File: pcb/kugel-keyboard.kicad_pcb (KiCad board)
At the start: 2 copper layers, 120.5 x 85.5 mm, 34 parts, among them SW1 MX_SW_HS, SW10 MX_SW_HS, SW11 MX_SW_HS, SW12 MX_SW_HS, SW13 MX_SW_HS, SW14 MX_SW_HS, SW15 MX_SW_HS, SW16 MX_SW_HS, SW17 MX_SW_HS, SW2 MX_SW_HS, SW3 MX_SW_HS, SW4 MX_SW_HS, SW5 MX_SW_HS, SW6 MX_SW_HS, SW7 MX_SW_HS, SW8 MX_SW_HS, SW9 MX_SW_HS

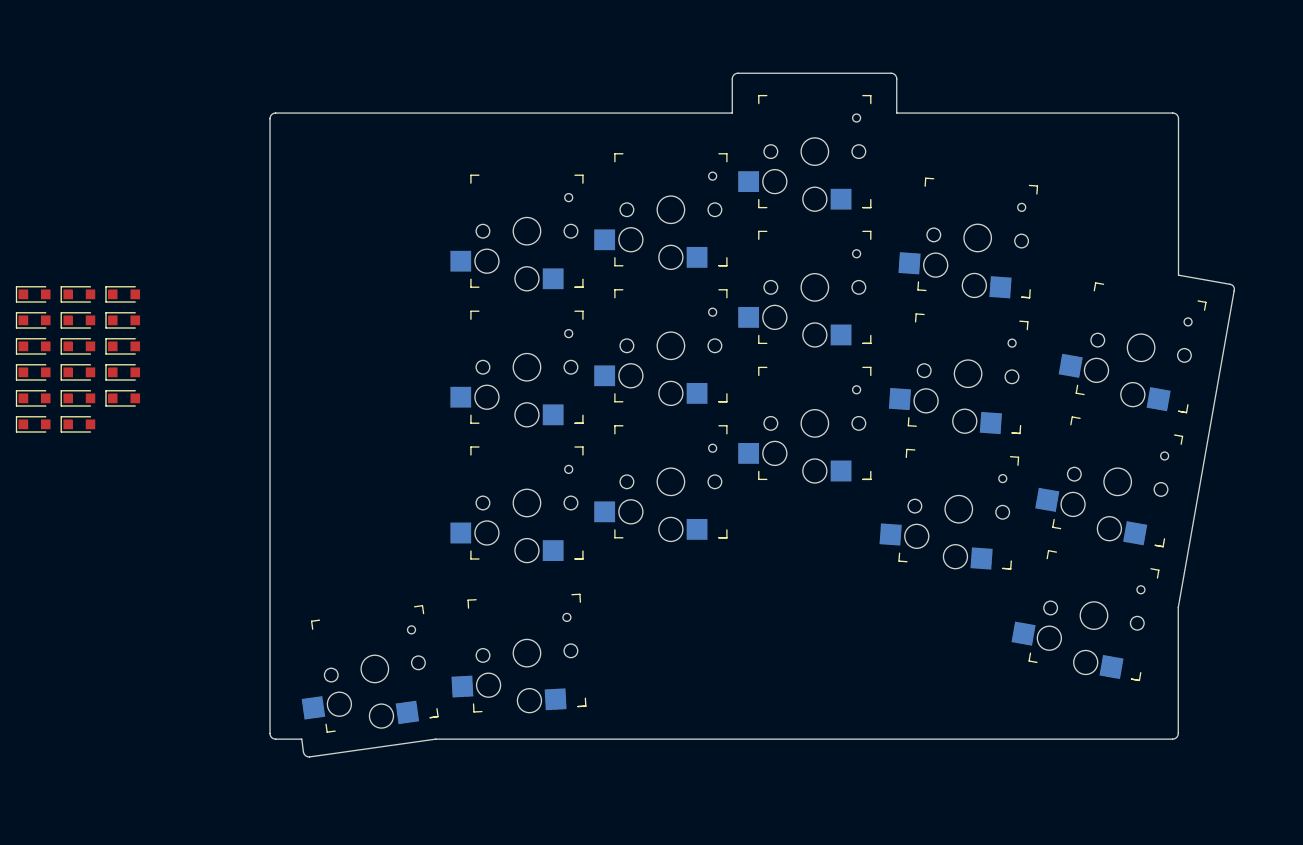
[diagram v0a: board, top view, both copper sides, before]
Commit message: added right side PCB and GPIO breakout PCB
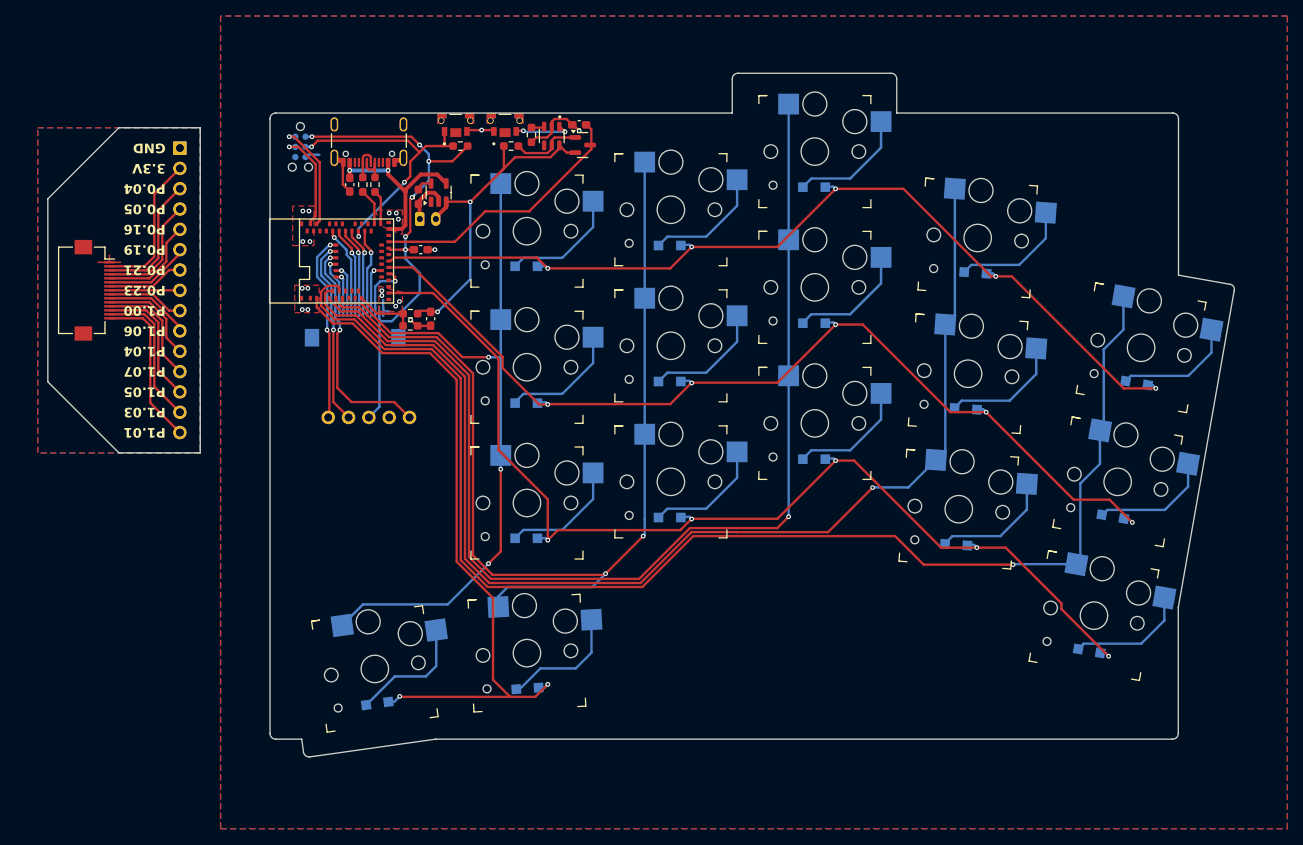
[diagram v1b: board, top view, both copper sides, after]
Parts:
- added C1: 10u, Capacitor_SMD:C_0603_1608Metric_Pad1.08x0.95mm_HandSolder, F.Cu at (117.8, 65.5)
- added C2: 10u, Capacitor_SMD:C_0603_1608Metric_Pad1.08x0.95mm_HandSolder, F.Cu at (127.9, 82.3)
- added C3: 10u, Capacitor_SMD:C_0603_1608Metric_Pad1.08x0.95mm_HandSolder, F.Cu at (126.6, 73.7)
- added C4: 10u, Capacitor_SMD:C_0603_1608Metric_Pad1.08x0.95mm_HandSolder, F.Cu at (146.4, 58.1)
- added J1: Conn_01x15_Pin, Connector_FFC-FPC:Hirose_FH12-15S-0.5SH_1x15-1MP_P0.50mm_Horizontal, F.Cu at (85.9, 78.7)
- added J2: USB_C_Receptacle_USB2.0_16P, Connector_USB:USB_C_Receptacle_GCT_USB4105-xx-A_16P_TopMnt_Horizontal, F.Cu at (120.1, 59.1)
- added J3: Conn_01x02_Socket, custom-libary:Battery_solder_pads, F.Cu at (126.5, 69.8)
- added J4: Conn_01x15_Pin, Connector_PinHeader_2.54mm:PinHeader_1x15_P2.54mm_Vertical, B.Cu at (96.5, 61.0)
- added J5: Conn_ARM_SWD_TagConnect_TC2030-NL, Connector:Tag-Connect_TC2030-IDC-NL_2x03_P1.27mm_Vertical, B.Cu at (111.6, 60.8)
- added J6: Conn_01x15_Pin, Connector_FFC-FPC:Hirose_FH12-15S-0.5SH_1x15-1MP_P0.50mm_Horizontal, B.Cu at (118.4, 83.3)
- added Q1: IRLML6402, Package_TO_SOT_SMD:SOT-23, F.Cu at (146.9, 60.6)
- added R1: 2k, Resistor_SMD:R_0603_1608Metric_Pad0.98x0.95mm_HandSolder, F.Cu at (126.3, 67.1)
- added R2: R, Resistor_SMD:R_0603_1608Metric_Pad0.98x0.95mm_HandSolder, F.Cu at (125.3, 81.7)
- added R3: R, Resistor_SMD:R_0603_1608Metric_Pad0.98x0.95mm_HandSolder, F.Cu at (125.3, 83.2)
- added R4: 27, Resistor_SMD:R_0603_1608Metric_Pad0.98x0.95mm_HandSolder, F.Cu at (120.9, 65.5)
- added R5: 27, Resistor_SMD:R_0603_1608Metric_Pad0.98x0.95mm_HandSolder, F.Cu at (119.4, 65.5)
- added R6: 100k, Resistor_SMD:R_0603_1608Metric_Pad0.98x0.95mm_HandSolder, F.Cu at (131.6, 60.7)
- added R7: 100k, Resistor_SMD:R_0603_1608Metric_Pad0.98x0.95mm_HandSolder, F.Cu at (140.5, 59.3)
- added R8: 100k, Resistor_SMD:R_0603_1608Metric_Pad0.98x0.95mm_HandSolder, F.Cu at (137.9, 60.7)
- added SW18: SW_Push, custom-libary:SW_TL6340AF160Q, F.Cu at (131.0, 57.5)
- added SW20: SW_Push, custom-libary:SW_TL6340AF160Q, F.Cu at (137.2, 57.5)
- added U1: MDBT50Q, custom-libary:MDBT50Q-1MV2, F.Cu at (123.2, 80.3)
- added U2: LTC4054ES5-4.2, Package_TO_SOT_SMD:TSOT-23-5, F.Cu at (128.9, 66.5)
- added U3: ~, custom-libary:nice!view, F.Cu at (115.1, 94.6)
- added U4: MAX16054AZT_T, custom-libary:SOT95P275X110-6N, F.Cu at (143.0, 59.5)
- D1, D10, D11, D12, D13, D14, D15, D16, D17, D2, D3, D4, D5, D6, D7, D8, D9: moved to B.Cu
- moved D15 126.7 mm to (216.1, 90.3), turned to 170 degrees
- moved D16 124.9 mm to (213.1, 107.0), turned to 170 degrees
- moved D17 124.7 mm to (210.2, 123.8), turned to 170 degrees
- moved D12 113.6 mm to (195.9, 76.6), turned to 176 degrees
- moved D14 107.7 mm to (193.6, 110.5), turned to 176 degrees
- moved D13 106.2 mm to (194.7, 93.6), turned to 176 degrees
- moved D9 94.0 mm to (175.8, 65.8), turned to 180 degrees
- moved D11 92.2 mm to (175.8, 99.8), turned to 180 degrees
- moved D10 92.1 mm to (175.8, 82.8), turned to 180 degrees
- moved D5 81.7 mm to (157.7, 73.1), turned to 180 degrees
- moved D6 79.6 mm to (157.7, 90.1), turned to 180 degrees
- moved D7 78.9 mm to (157.7, 107.1), turned to 180 degrees
- moved D8 72.5 mm to (140.0, 128.5), turned to -176 degrees
- moved D3 66.0 mm to (139.8, 109.7), turned to 180 degrees
- moved D2 62.3 mm to (139.8, 92.8), turned to 180 degrees
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- renumbered SW8 to SW10, SW13 to SW11, SW4 to SW12, SW9 to SW13, SW5 to SW15, SW10 to SW16, SW15 to SW17, SW6 to SW2, SW11 to SW3, SW16 to SW4, SW2 to SW5, SW7 to SW6, SW12 to SW7, SW17 to SW8, SW3 to SW9
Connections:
- SW10 pad 1: col3 -> col2
- SW10 pad 2: Net-(D8-A) -> Net-(D10-A)
- SW11 pad 1: col1 -> col2
- SW11 pad 2: Net-(D13-A) -> Net-(D11-A)
- SW12 pad 1: col4 -> col1
- SW12 pad 2: Net-(D4-A) -> Net-(D12-A)
- SW13 pad 1: col2 -> col1
- SW13 pad 2: Net-(D9-A) -> Net-(D13-A)
- SW15 pad 1: col3 -> col0
- SW15 pad 2: Net-(D5-A) -> Net-(D15-A)
- SW16 pad 1: col2 -> col0
- SW16 pad 2: Net-(D10-A) -> Net-(D16-A)
- SW17 pad 2: Net-(D15-A) -> Net-(D17-A)
- SW2 pad 1: col3 -> col4
- SW2 pad 2: Net-(D6-A) -> Net-(D2-A)
- SW3 pad 1: col2 -> col4
- SW3 pad 2: Net-(D11-A) -> Net-(D3-A)
- SW4 pad 1: col0 -> col4
- SW4 pad 2: Net-(D16-A) -> Net-(D4-A)
- SW5 pad 1: col4 -> col3
- SW5 pad 2: Net-(D2-A) -> Net-(D5-A)
- SW6 pad 2: Net-(D7-A) -> Net-(D6-A)
- SW7 pad 1: col1 -> col3
- SW7 pad 2: Net-(D12-A) -> Net-(D7-A)
- SW8 pad 1: col0 -> col3
- SW8 pad 2: Net-(D17-A) -> Net-(D8-A)
- SW9 pad 1: col4 -> col2
- SW9 pad 2: Net-(D3-A) -> Net-(D9-A)
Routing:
- net col0: track 0.00 -> 167.2 mm, vias 0 -> 1
- net col1: track 0.00 -> 147.8 mm, vias 0 -> 1
- net col2: track 0.00 -> 140.2 mm, vias 0 -> 1
- net row2: track 0.00 -> 133.8 mm, vias 0 -> 5
- net col3: track 0.00 -> 131.0 mm, vias 0 -> 2
- net row1: track 0.00 -> 121.9 mm, vias 0 -> 5
- net row0: track 0.00 -> 117.7 mm, vias 0 -> 5
- net col4: track 0.00 -> 92.9 mm, vias 0 -> 3
- net row3: track 0.00 -> 87.0 mm, vias 0 -> 2
- net +3.3V: track 0.00 -> 64.9 mm, vias 0 -> 6
- net /VBAT: track 0.00 -> 43.9 mm, vias 0 -> 2
- net /RST: track 0.00 -> 36.0 mm, vias 0 -> 3
- net /VSWITCHED: track 0.00 -> 33.4 mm
- net GND: track 0.00 -> 33.4 mm, vias 0 -> 19
- net /P1.05: track 0.00 -> 28.9 mm, vias 0 -> 2
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- added copper zone on F.Cu, net (none)
- added copper zone on B.Cu, net GND
- added copper zone on F.Cu, net GND
- added copper zone on B.Cu, net Net-(J1-Pin_1)
- added copper zone on F.Cu, net Net-(J1-Pin_1)
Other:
- board size 120.5 x 85.5 mm -> 148.3 x 85.5 mm
- board text added: "3.3V"
- board text added: "GND"
- board text added: "P0.04"
- board text added: "P0.05"
- board text added: "P0.16"
- board text added: "P0.19"
- board text added: "P0.21"
- board text added: "P0.23"
- board text added: "P1.00"
- board text added: "P1.01"
- board text added: "P1.03"
- board text added: "P1.04"
- board text added: "P1.05"
- board text added: "P1.06"
- board text added: "P1.07"
